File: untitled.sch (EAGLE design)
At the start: 27 parts, among them IC1 ACS758LCB-050B-PFF-T, IC2 LM2936DT-3.3

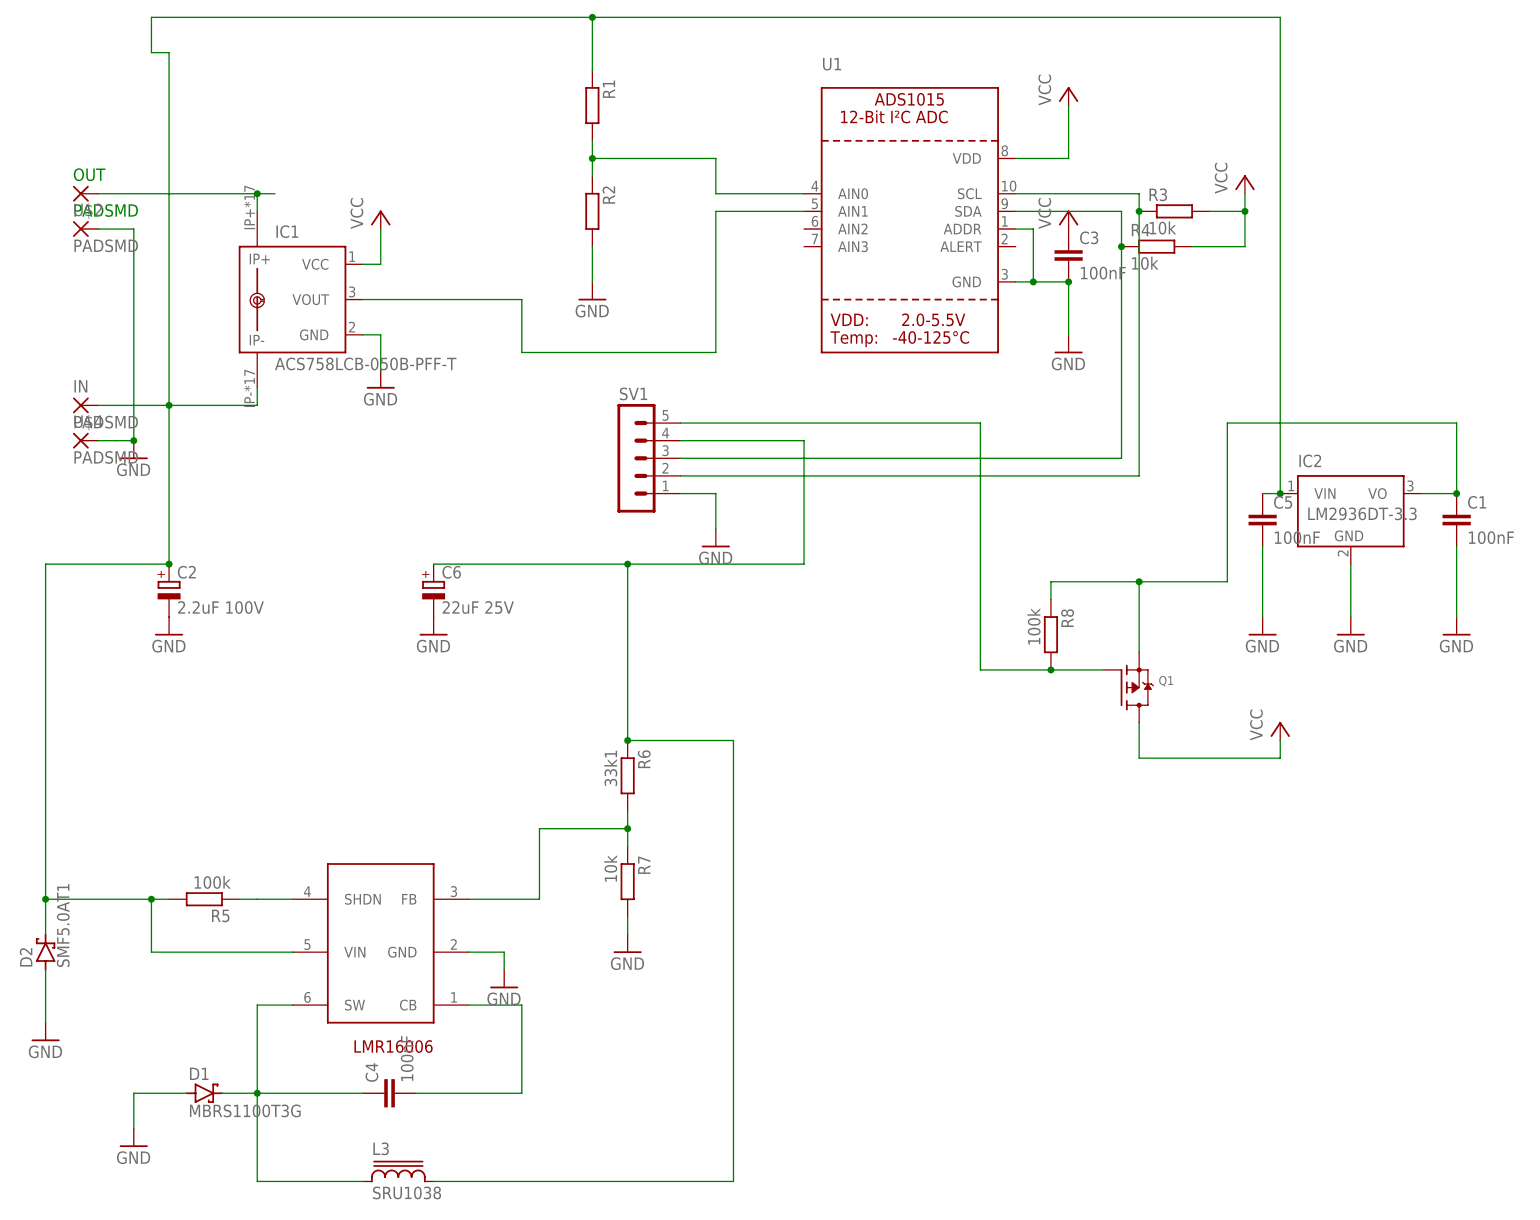
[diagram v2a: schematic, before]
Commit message: Use smaller current sensor and update schematic
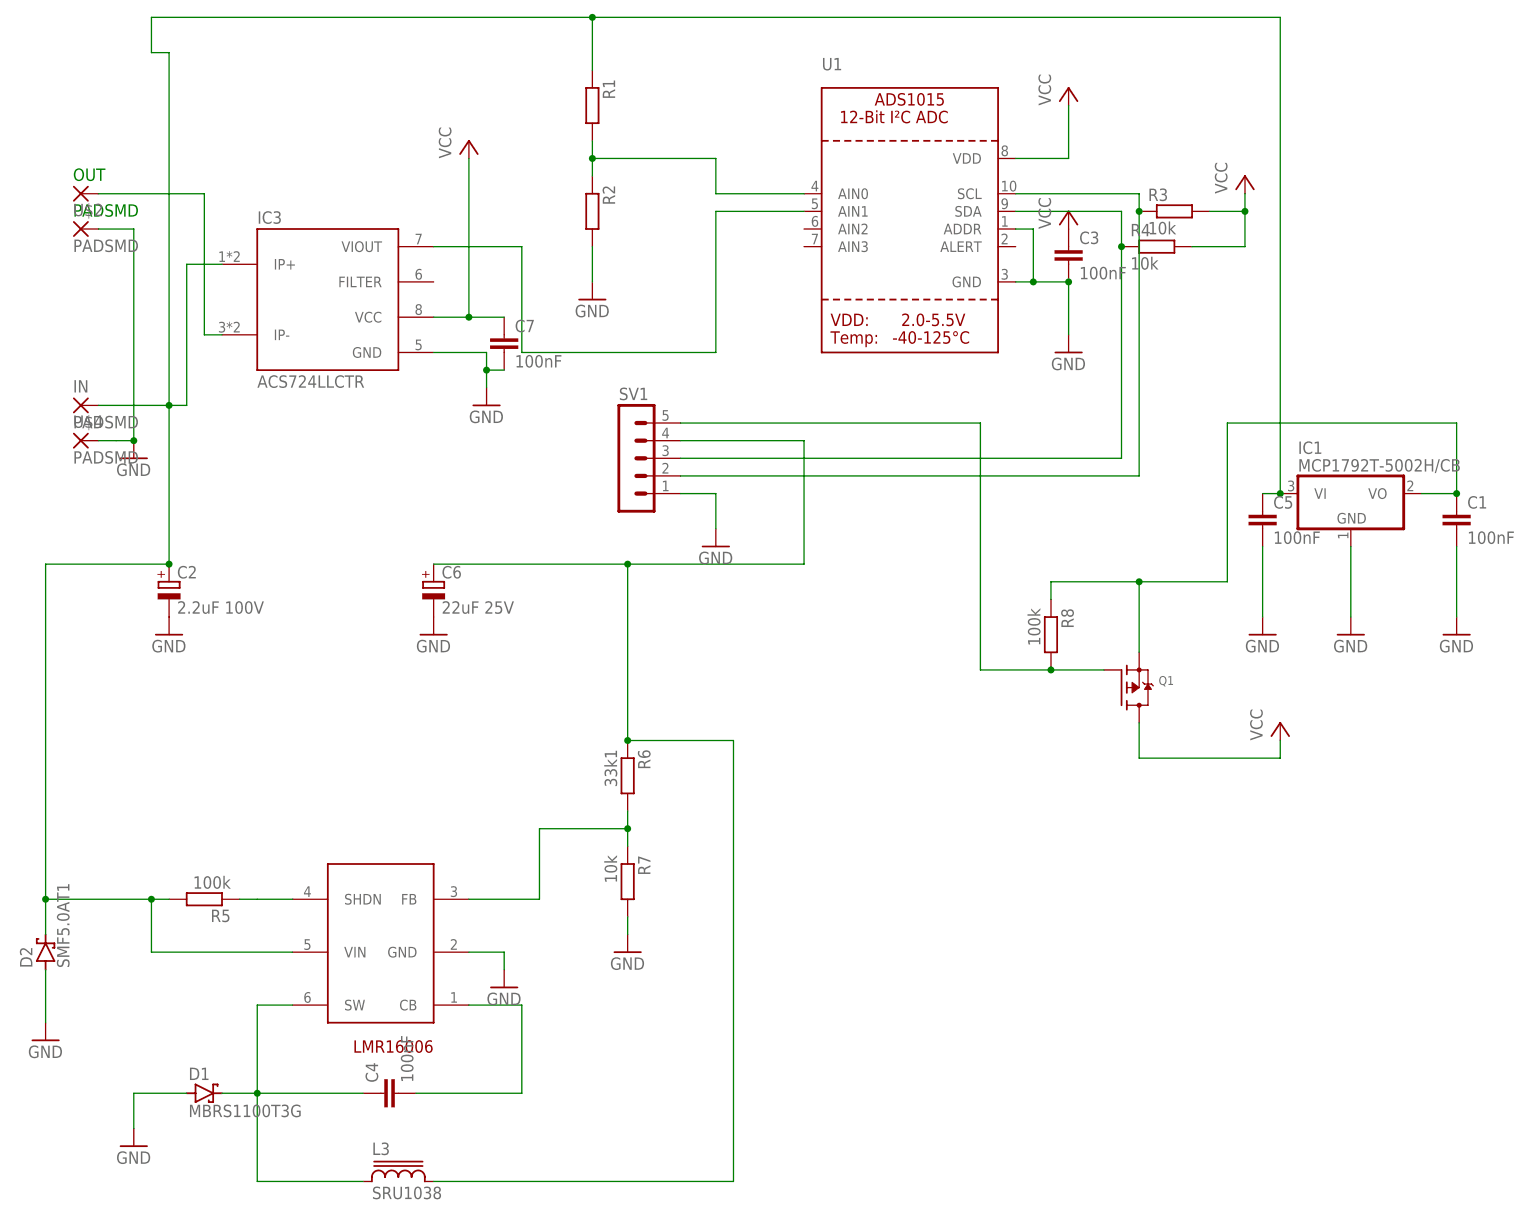
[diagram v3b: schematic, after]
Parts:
- removed IC2: LM2936DT-3.3, national-semiconductor:LM2936DT-3.3
- added C7: 100nF, rcl:C-EUC0805
- added IC3: ACS724LLCTR, we-sensor:ACS724LLCTR
- IC1: value ACS758LCB-050B-PFF-T -> MCP1792T-5002H/CB; device allegro:ACS758LCB-050B-PFF-T -> linear:MCP1703CB
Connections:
- net GND: now also C7.2, IC3.GND; no longer IC2.GND
- net N$1: now also IC3.VIOUT; no longer IC1.VOUT
- net N$12: now also IC1.VO; no longer IC2.VO
- net N$2: now also IC3.IP-; no longer IC1.IP+
- net N$4: now also IC1.VI, IC3.IP+; no longer IC1.IP-, IC2.VIN
- net VCC: now also C7.1, IC3.VCC; no longer IC1.VCC
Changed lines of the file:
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@@
 </classes>
 <parts>
-<part name="IC1" library="allegro" library_urn="urn:adsk.eagle:library:93" deviceset="ACS758*" device="" package3d_urn="urn:adsk.eagle:package:3449/1" technology="LCB-050B-PFF-T"/>
 <part name="U1" library="microbuilder" deviceset="ADC_ADS1015" device=""/>
 <part name="R1" library="rcl" library_urn="urn:adsk.eagle:library:334" deviceset="R-EU_" device="R0805" package3d_urn="urn:adsk.eagle:package:23553/2"/>
@@
 <part name="R8" library="rcl" library_urn="urn:adsk.eagle:library:334" deviceset="R-EU_" device="R0805" package3d_urn="urn:adsk.eagle:package:23553/2" value="100k"/>
 <part name="P+2" library="supply1" library_urn="urn:adsk.eagle:library:371" deviceset="VCC" device=""/>
-<part name="IC2" library="national-semiconductor" library_urn="urn:adsk.eagle:library:307" deviceset="LM2936?*" device="DT" package3d_urn="urn:adsk.eagle:package:21225/1" technology="-3.3"/>
 <part name="GND12" library="supply1" library_urn="urn:adsk.eagle:library:371" deviceset="GND" device=""/>
 <part name="C1" library="rcl" library_urn="urn:adsk.eagle:library:334" deviceset="C-EU" device="C0805" package3d_urn="urn:adsk.eagle:package:23617/2" value="100nF"/>
@@
 <part name="C5" library="rcl" library_urn="urn:adsk.eagle:library:334" deviceset="C-EU" device="C0805" package3d_urn="urn:adsk.eagle:package:23617/2" value="100nF"/>
 <part name="GND14" library="supply1" library_urn="urn:adsk.eagle:library:371" deviceset="GND" device=""/>
+<part name="IC3" library="we-sensor" deviceset="ACS724" device="LLCTR"/>
+<part name="IC1" library="linear" library_urn="urn:adsk.eagle:library:262" deviceset="MCP1703" device="CB" package3d_urn="urn:adsk.eagle:package:16489/2" value="MCP1792T-5002H/CB"/>
+<part name="C7" library="rcl" library_urn="urn:adsk.eagle:library:334" deviceset="C-EU" device="C0805" package3d_urn="urn:adsk.eagle:package:23617/2" value="100nF"/>
 </parts>
 <sheets>
@@
 </plain>
 <instances>
-<instance part="IC1" gate="G$1" x="25.4" y="76.2" smashed="yes">
-<attribute name="NAME" x="22.86" y="85.09" size="1.778" layer="95"/>
-<attribute name="VALUE" x="22.86" y="66.04" size="1.778" layer="96"/>
-</instance>
 <instance part="U1" gate="G$1" x="114.3" y="88.9" smashed="yes">
 <attribute name="NAME" x="101.6" y="109.22" size="1.778" layer="95"/>
@@
 <attribute name="VALUE" x="66.04" y="73.66" size="1.778" layer="96"/>
 </instance>
-<instance part="GND5" gate="1" x="38.1" y="63.5" smashed="yes">
-<attribute name="VALUE" x="35.56" y="60.96" size="1.778" layer="96"/>
+<instance part="GND5" gate="1" x="53.34" y="60.96" smashed="yes">
+<attribute name="VALUE" x="50.8" y="58.42" size="1.778" layer="96"/>
 </instance>
 <instance part="P+1" gate="VCC" x="137.16" y="106.68" smashed="yes">
 <attribute name="VALUE" x="134.62" y="104.14" size="1.778" layer="96" rot="R90"/>
 </instance>
-<instance part="P+4" gate="VCC" x="38.1" y="88.9" smashed="yes">
-<attribute name="VALUE" x="35.56" y="86.36" size="1.778" layer="96" rot="R90"/>
+<instance part="P+4" gate="VCC" x="50.8" y="99.06" smashed="yes">
+<attribute name="VALUE" x="48.26" y="96.52" size="1.778" layer="96" rot="R90"/>
 </instance>
 <instance part="R3" gate="G$1" x="152.4" y="88.9" smashed="yes">
@@
 <attribute name="VALUE" x="165.1" y="12.7" size="1.778" layer="96" rot="R90"/>
 </instance>
-<instance part="IC2" gate="G$1" x="177.8" y="45.72" smashed="yes">
-<attribute name="NAME" x="170.18" y="52.07" size="1.778" layer="95"/>
-<attribute name="VALUE" x="171.45" y="44.45" size="1.778" layer="96"/>
-</instance>
 <instance part="GND12" gate="1" x="177.8" y="27.94" smashed="yes">
 <attribute name="VALUE" x="175.26" y="25.4" size="1.778" layer="96"/>
@@
 <instance part="GND14" gate="1" x="165.1" y="27.94" smashed="yes">
 <attribute name="VALUE" x="162.56" y="25.4" size="1.778" layer="96"/>
+</instance>
+<instance part="IC3" gate="IC" x="30.48" y="76.2" smashed="yes">
+<attribute name="NAME" x="20.32" y="88.9" size="1.778" layer="95" align="top-left"/>
+<attribute name="VALUE" x="20.32" y="63.5" size="1.778" layer="96"/>
+</instance>
+<instance part="IC1" gate="G$1" x="177.8" y="48.26" smashed="yes">
+<attribute name="NAME" x="170.18" y="53.975" size="1.778" layer="95"/>
+<attribute name="VALUE" x="170.18" y="51.435" size="1.778" layer="96"/>
+</instance>
+<instance part="C7" gate="G$1" x="55.88" y="71.12" smashed="yes">
+<attribute name="NAME" x="57.404" y="71.501" size="1.778" layer="95"/>
+<attribute name="VALUE" x="57.404" y="66.421" size="1.778" layer="96"/>
 </instance>
 </instances>
@@
 </segment>
 <segment>
-<pinref part="IC1" gate="G$1" pin="VCC"/>
-<wire x1="35.56" y1="81.28" x2="38.1" y2="81.28" width="0.1524" layer="91"/>
-<wire x1="38.1" y1="81.28" x2="38.1" y2="86.36" width="0.1524" layer="91"/>
+<wire x1="45.72" y1="73.66" x2="50.8" y2="73.66" width="0.1524" layer="91"/>
+<wire x1="50.8" y1="73.66" x2="50.8" y2="96.52" width="0.1524" layer="91"/>
 <pinref part="P+4" gate="VCC" pin="VCC"/>
+<pinref part="IC3" gate="IC" pin="VCC"/>
+<pinref part="C7" gate="G$1" pin="1"/>
+<wire x1="55.88" y1="73.66" x2="50.8" y2="73.66" width="0.1524" layer="91"/>
+<junction x="50.8" y="73.66"/>
 </segment>
 <segment>
@@
 </segment>
 <segment>
-<pinref part="IC1" gate="G$1" pin="GND"/>
-<wire x1="35.56" y1="71.12" x2="38.1" y2="71.12" width="0.1524" layer="91"/>
-<wire x1="38.1" y1="71.12" x2="38.1" y2="66.04" width="0.1524" layer="91"/>
+<wire x1="45.72" y1="68.58" x2="53.34" y2="68.58" width="0.1524" layer="91"/>
+<wire x1="53.34" y1="68.58" x2="53.34" y2="66.04" width="0.1524" layer="91"/>
 <pinref part="GND5" gate="1" pin="GND"/>
+<pinref part="IC3" gate="IC" pin="GND"/>
+<pinref part="C7" gate="G$1" pin="2"/>
+<wire x1="53.34" y1="66.04" x2="53.34" y2="63.5" width="0.1524" layer="91"/>
+<wire x1="55.88" y1="66.04" x2="53.34" y2="66.04" width="0.1524" layer="91"/>
+<junction x="53.34" y="66.04"/>
 </segment>
 <segment>
@@
 </segment>
 <segment>
-<pinref part="IC2" gate="G$1" pin="GND"/>
-<wire x1="177.8" y1="38.1" x2="177.8" y2="30.48" width="0.1524" layer="91"/>
+<wire x1="177.8" y1="40.64" x2="177.8" y2="30.48" width="0.1524" layer="91"/>
 <pinref part="GND12" gate="1" pin="GND"/>
+<pinref part="IC1" gate="G$1" pin="GND"/>
 </segment>
 <segment>
@@
 <net name="N$1" class="0">
 <segment>
-<pinref part="IC1" gate="G$1" pin="VOUT"/>
-<wire x1="35.56" y1="76.2" x2="58.42" y2="76.2" width="0.1524" layer="91"/>
-<wire x1="58.42" y1="76.2" x2="58.42" y2="68.58" width="0.1524" layer="91"/>
+<wire x1="45.72" y1="83.82" x2="58.42" y2="83.82" width="0.1524" layer="91"/>
+<wire x1="58.42" y1="83.82" x2="58.42" y2="68.58" width="0.1524" layer="91"/>
 <wire x1="58.42" y1="68.58" x2="86.36" y2="68.58" width="0.1524" layer="91"/>
 <wire x1="86.36" y1="68.58" x2="86.36" y2="88.9" width="0.1524" layer="91"/>
 <pinref part="U1" gate="G$1" pin="AIN1"/>
 <wire x1="86.36" y1="88.9" x2="99.06" y2="88.9" width="0.1524" layer="91"/>
+<pinref part="IC3" gate="IC" pin="VIOUT"/>
 </segment>
 </net>
@@
 <segment>
 <wire x1="-2.54" y1="60.96" x2="7.62" y2="60.96" width="0.1524" layer="91"/>
-<pinref part="IC1" gate="G$1" pin="IP-"/>
-<wire x1="7.62" y1="60.96" x2="20.32" y2="60.96" width="0.1524" layer="91"/>
-<wire x1="20.32" y1="60.96" x2="20.32" y2="63.5" width="0.1524" layer="91"/>
+<wire x1="7.62" y1="60.96" x2="10.16" y2="60.96" width="0.1524" layer="91"/>
 <wire x1="7.62" y1="60.96" x2="7.62" y2="111.76" width="0.1524" layer="91"/>
 <wire x1="7.62" y1="111.76" x2="5.08" y2="111.76" width="0.1524" layer="91"/>
@@
 <wire x1="-10.16" y1="-10.16" x2="-10.16" y2="-15.24" width="0.1524" layer="91"/>
 <junction x="-10.16" y="-10.16"/>
-<pinref part="IC2" gate="G$1" pin="VIN"/>
 <wire x1="167.64" y1="48.26" x2="167.64" y2="116.84" width="0.1524" layer="91"/>
 <wire x1="167.64" y1="116.84" x2="68.58" y2="116.84" width="0.1524" layer="91"/>
@@
 <pinref part="C5" gate="G$1" pin="1"/>
 <wire x1="167.64" y1="48.26" x2="165.1" y2="48.26" width="0.1524" layer="91"/>
+<wire x1="10.16" y1="60.96" x2="10.16" y2="81.28" width="0.1524" layer="91"/>
+<pinref part="IC3" gate="IC" pin="IP+"/>
+<wire x1="10.16" y1="81.28" x2="15.24" y2="81.28" width="0.1524" layer="91"/>
+<pinref part="IC1" gate="G$1" pin="VI"/>
 <junction x="167.64" y="48.26"/>
 </segment>
@@
 <net name="N$2" class="0">
 <segment>
-<pinref part="IC1" gate="G$1" pin="IP+"/>
-<wire x1="20.32" y1="88.9" x2="20.32" y2="91.44" width="0.1524" layer="91"/>
-<wire x1="20.32" y1="91.44" x2="22.86" y2="91.44" width="0.1524" layer="91"/>
-<junction x="20.32" y="91.44"/>
-<wire x1="-2.54" y1="91.44" x2="20.32" y2="91.44" width="0.1524" layer="91"/>
+<wire x1="-2.54" y1="91.44" x2="12.7" y2="91.44" width="0.1524" layer="91"/>
 <pinref part="OUT" gate="G$1" pin="P"/>
+<pinref part="IC3" gate="IC" pin="IP-"/>
+<wire x1="15.24" y1="71.12" x2="12.7" y2="71.12" width="0.1524" layer="91"/>
+<wire x1="12.7" y1="71.12" x2="12.7" y2="91.44" width="0.1524" layer="91"/>
 </segment>
 </net>
@@
 <wire x1="160.02" y1="58.42" x2="193.04" y2="58.42" width="0.1524" layer="91"/>
 <wire x1="193.04" y1="58.42" x2="193.04" y2="48.26" width="0.1524" layer="91"/>
-<pinref part="IC2" gate="G$1" pin="VO"/>
 <wire x1="193.04" y1="48.26" x2="187.96" y2="48.26" width="0.1524" layer="91"/>
 <pinref part="C1" gate="G$1" pin="1"/>
 <junction x="193.04" y="48.26"/>
-</segment>
-</net>
+<pinref part="IC1" gate="G$1" pin="VO"/>
+</segment>
+</net>
